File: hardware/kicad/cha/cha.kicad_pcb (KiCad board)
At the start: 4 copper layers, 173 x 134 mm, 137 parts, among them J1 AES_CHA, J2 CONF C, J3 CONF SM, J4 microSD, J5 Câble PROG-CHA, SW1 Retour menu, U1 AMS1117-3.3, U10 74AHCT1G32, U11 74LVC1G07, U12 iCE40HX4K-TQ144, U13 AS4C32M16SB-6TIN, U14 iCE40HX4K-TQ144, U15 IS61WV10248EDBLL-10TLI, U2 AP2112K-1.2, U3 74LVC16244A, U4 74LVC16244A, U5 74LVC16244A, U6 74LVC16244A, U7 74AHCT16244, U8 74AHCT16244, U9 74AHCT244, X1 25 MHz 3,3 V, X2 25 MHz 3,3 V

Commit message: PCB : carte PROG entièrement routée ; CHA à 2 liaisons (DOTA, GAD0)
Routeur de finition : PROG -> dernier raccordement (+3V3 de C46) fait,
plus aucune liaison manquante ; CHA -> P4 routé (et réseaux voisins
rerouttés), restent DOTA et GAD0 dont les broches d'entrée du tampon U7
sont enfermées par les pistes FIXD qui longent sa rangée. DRC des deux
cartes : aucune violation d'isolement ni court-circuit (restent
sérigraphie et bibliothèque non déclarée dans l'environnement).

Co-Authored-By: Claude Opus 5.5 <noreply@anthropic.com>
Claude-Session: https://claude.ai/code/session_01WKfXP1YJ8otGxZ5dsY6Agh
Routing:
- net P4: track 55.6 -> 133.4 mm, vias 2 -> 8
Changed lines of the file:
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@@
   (segment (start 161.5976 95.9844) (end 163.332 94.25) (width 0.127) (layer "B.Cu") (net 193))
   (segment (start 154.235 133.2133) (end 153.7111 133.2133) (width 0.127) (layer "B.Cu") (net 193))
+  (segment (start 121.762499 94.85) (end 121.6625 94.95) (width 0.127) (layer "F.Cu") (net 194))
   (segment (start 181.3375 96.75) (end 181.2283 96.8592) (width 0.127) (layer "F.Cu") (net 194))
   (segment (start 177.5821 128.5995) (end 177.8187 128.8361) (width 0.127) (layer "F.Cu") (net 194))
+  (segment (start 121.9625 94.85) (end 121.762499 94.85) (width 0.127) (layer "F.Cu") (net 194))
+  (segment (start 160.0625 130.05) (end 160.2625 130.05) (width 0.127) (layer "F.Cu") (net 194))
+  (segment (start 121.6625 94.95) (end 121.6625 95.05) (width 0.127) (layer "F.Cu") (net 194))
   (segment (start 161.7792 128.5995) (end 177.5821 128.5995) (width 0.127) (layer "F.Cu") (net 194))
+  (segment (start 134.1625 117.85) (end 134.3625 118.05) (width 0.127) (layer "F.Cu") (net 194))
   (segment (start 181.2283 96.8592) (end 177.5482 96.8592) (width 0.127) (layer "F.Cu") (net 194))
   (segment (start 159.75 130.6287) (end 161.7792 128.5995) (width 0.127) (layer "F.Cu") (net 194))
+  (segment (start 121.5625 103.65) (end 121.5625 105.75) (width 0.127) (layer "F.Cu") (net 194))
+  (segment (start 120.9625 103.05) (end 121.5625 103.65) (width 0.127) (layer "F.Cu") (net 194))
+  (segment (start 121.6625 95.05) (end 121.1625 95.55) (width 0.127) (layer "F.Cu") (net 194))
+  (segment (start 124.262499 117.85) (end 134.1625 117.85) (width 0.127) (layer "F.Cu") (net 194))
+  (segment (start 121.5625 105.75) (end 121.4625 105.85) (width 0.127) (layer "F.Cu") (net 194))
   (segment (start 159.75 131.2875) (end 159.75 130.6287) (width 0.127) (layer "F.Cu") (net 194))
+  (via (at 160.0625 130.05) (size 0.6) (drill 0.3) (layers "F.Cu" "B.Cu") (net 194))
+  (via (at 120.9625 103.05) (size 0.6) (drill 0.3) (layers "F.Cu" "B.Cu") (net 194))
+  (via (at 124.262499 117.85) (size 0.6) (drill 0.3) (layers "F.Cu" "B.Cu") (net 194))
+  (via (at 121.1625 95.55) (size 0.6) (drill 0.3) (layers "F.Cu" "B.Cu") (net 194))
   (via (at 177.8187 128.8361) (size 0.6) (drill 0.3) (layers "F.Cu" "B.Cu") (net 194))
   (via (at 177.5482 96.8592) (size 0.6) (drill 0.3) (layers "F.Cu" "B.Cu") (net 194))
+  (via (at 121.4625 105.85) (size 0.6) (drill 0.3) (layers "F.Cu" "B.Cu") (net 194))
+  (via (at 134.3625 118.05) (size 0.6) (drill 0.3) (layers "F.Cu" "B.Cu") (net 194))
+  (segment (start 158.5625 130.75) (end 158.6625 130.65) (width 0.127) (layer "B.Cu") (net 194))
+  (segment (start 120.9625 97.45) (end 120.8625 97.55) (width 0.127) (layer "B.Cu") (net 194))
+  (segment (start 124.262499 117.25) (end 124.262499 117.85) (width 0.127) (layer "B.Cu") (net 194))
+  (segment (start 156.462499 131.85) (end 156.5625 131.75) (width 0.127) (layer "B.Cu") (net 194))
+  (segment (start 157.0625 131.55) (end 157.1625 131.449999) (width 0.127) (layer "B.Cu") (net 194))
+  (segment (start 120.8625 97.55) (end 120.8625 100.55) (width 0.127) (layer "B.Cu") (net 194))
+  (segment (start 160.0625 130.15) (end 160.0625 130.05) (width 0.127) (layer "B.Cu") (net 194))
+  (segment (start 158.1625 130.949999) (end 158.2625 130.85) (width 0.127) (layer "B.Cu") (net 194))
+  (segment (start 121.4625 105.85) (end 120.1625 107.15) (width 0.127) (layer "B.Cu") (net 194))
+  (segment (start 120.9625 95.95) (end 120.9625 97.45) (width 0.127) (layer "B.Cu") (net 194))
+  (segment (start 139.2625 133.449999) (end 142.9625 133.449999) (width 0.127) (layer "B.Cu") (net 194))
+  (segment (start 154.5625 133.75) (end 155.2625 133.05) (width 0.127) (layer "B.Cu") (net 194))
+  (segment (start 143.2625 133.75) (end 143.3625 133.75) (width 0.127) (layer "B.Cu") (net 194))
+  (segment (start 120.9625 100.65) (end 120.9625 103.05) (width 0.127) (layer "B.Cu") (net 194))
+  (segment (start 158.462499 130.75) (end 158.5625 130.75) (width 0.127) (layer "B.Cu") (net 194))
+  (segment (start 156.1625 132.449999) (end 156.1625 132.05) (width 0.127) (layer "B.Cu") (net 194))
+  (segment (start 137.0625 130.35) (end 137.1625 130.449999) (width 0.127) (layer "B.Cu") (net 194))
+  (segment (start 143.3625 133.85) (end 152.5625 133.85) (width 0.127) (layer "B.Cu") (net 194))
+  (segment (start 122.6625 115.65) (end 124.262499 117.25) (width 0.127) (layer "B.Cu") (net 194))
+  (segment (start 121.1625 95.75) (end 120.9625 95.95) (width 0.127) (layer "B.Cu") (net 194))
+  (segment (start 159.5625 130.55) (end 159.6625 130.55) (width 0.127) (layer "B.Cu") (net 194))
+  (segment (start 156.6625 131.75) (end 156.7625 131.65) (width 0.127) (layer "B.Cu") (net 194))
+  (segment (start 156.3625 131.85) (end 156.462499 131.85) (width 0.127) (layer "B.Cu") (net 194))
+  (segment (start 121.1625 95.55) (end 121.1625 95.75) (width 0.127) (layer "B.Cu") (net 194))
+  (segment (start 157.3625 131.35) (end 157.462499 131.35) (width 0.127) (layer "B.Cu") (net 194))
+  (segment (start 159.4625 130.65) (end 159.5625 130.55) (width 0.127) (layer "B.Cu") (net 194))
+  (segment (start 134.3625 118.05) (end 134.7625 118.45) (width 0.127) (layer "B.Cu") (net 194))
+  (segment (start 155.2625 133.05) (end 155.5625 133.05) (width 0.127) (layer "B.Cu") (net 194))
+  (segment (start 134.7625 118.45) (end 134.7625 127.75) (width 0.127) (layer "B.Cu") (net 194))
+  (segment (start 120.1625 107.15) (end 120.1625 113.15) (width 0.127) (layer "B.Cu") (net 194))
+  (segment (start 156.7625 131.65) (end 156.8625 131.65) (width 0.127) (layer "B.Cu") (net 194))
+  (segment (start 156.962499 131.55) (end 157.0625 131.55) (width 0.127) (layer "B.Cu") (net 194))
+  (segment (start 156.5625 131.75) (end 156.6625 131.75) (width 0.127) (layer "B.Cu") (net 194))
+  (segment (start 121.9625 113.25) (end 122.6625 113.95) (width 0.127) (layer "B.Cu") (net 194))
+  (segment (start 143.3625 133.75) (end 143.3625 133.85) (width 0.127) (layer "B.Cu") (net 194))
+  (segment (start 157.2625 131.449999) (end 157.3625 131.35) (width 0.127) (layer "B.Cu") (net 194))
+  (segment (start 157.7625 131.15) (end 157.8625 131.15) (width 0.127) (layer "B.Cu") (net 194))
+  (segment (start 120.1625 113.15) (end 120.262499 113.25) (width 0.127) (layer "B.Cu") (net 194))
+  (segment (start 142.9625 133.449999) (end 143.2625 133.75) (width 0.127) (layer "B.Cu") (net 194))
+  (segment (start 158.6625 130.65) (end 159.4625 130.65) (width 0.127) (layer "B.Cu") (net 194))
+  (segment (start 157.8625 131.15) (end 158.0625 130.949999) (width 0.127) (layer "B.Cu") (net 194))
   (segment (start 177.8187 128.8361) (end 177.5482 128.5656) (width 0.127) (layer "B.Cu") (net 194))
+  (segment (start 158.0625 130.949999) (end 158.1625 130.949999) (width 0.127) (layer "B.Cu") (net 194))
+  (segment (start 137.0625 130.05) (end 137.0625 130.35) (width 0.127) (layer "B.Cu") (net 194))
+  (segment (start 156.1625 132.05) (end 156.3625 131.85) (width 0.127) (layer "B.Cu") (net 194))
+  (segment (start 156.8625 131.65) (end 156.962499 131.55) (width 0.127) (layer "B.Cu") (net 194))
+  (segment (start 139.1625 132.55) (end 139.1625 133.35) (width 0.127) (layer "B.Cu") (net 194))
+  (segment (start 155.5625 133.05) (end 156.1625 132.449999) (width 0.127) (layer "B.Cu") (net 194))
+  (segment (start 139.1625 133.35) (end 139.2625 133.449999) (width 0.127) (layer "B.Cu") (net 194))
+  (segment (start 158.2625 130.85) (end 158.3625 130.85) (width 0.127) (layer "B.Cu") (net 194))
+  (segment (start 120.8625 100.55) (end 120.9625 100.65) (width 0.127) (layer "B.Cu") (net 194))
+  (segment (start 137.1625 130.55) (end 139.1625 132.55) (width 0.127) (layer "B.Cu") (net 194))
+  (segment (start 152.5625 133.85) (end 152.6625 133.75) (width 0.127) (layer "B.Cu") (net 194))
   (segment (start 177.5482 128.5656) (end 177.5482 96.8592) (width 0.127) (layer "B.Cu") (net 194))
+  (segment (start 157.5625 131.25) (end 157.6625 131.25) (width 0.127) (layer "B.Cu") (net 194))
+  (segment (start 158.3625 130.85) (end 158.462499 130.75) (width 0.127) (layer "B.Cu") (net 194))
+  (segment (start 122.6625 113.95) (end 122.6625 115.65) (width 0.127) (layer "B.Cu") (net 194))
+  (segment (start 157.462499 131.35) (end 157.5625 131.25) (width 0.127) (layer "B.Cu") (net 194))
+  (segment (start 137.1625 130.449999) (end 137.1625 130.55) (width 0.127) (layer "B.Cu") (net 194))
+  (segment (start 134.7625 127.75) (end 137.0625 130.05) (width 0.127) (layer "B.Cu") (net 194))
+  (segment (start 152.6625 133.75) (end 154.5625 133.75) (width 0.127) (layer "B.Cu") (net 194))
+  (segment (start 157.1625 131.449999) (end 157.2625 131.449999) (width 0.127) (layer "B.Cu") (net 194))
+  (segment (start 120.262499 113.25) (end 121.9625 113.25) (width 0.127) (layer "B.Cu") (net 194))
+  (segment (start 157.6625 131.25) (end 157.7625 131.15) (width 0.127) (layer "B.Cu") (net 194))
+  (segment (start 159.6625 130.55) (end 160.0625 130.15) (width 0.127) (layer "B.Cu") (net 194))
   (segment (start 158.75 131.2875) (end 158.75 130.2322) (width 0.127) (layer "F.Cu") (net 195))
   (segment (start 165.1318 95.2812) (end 165.3767 95.0363) (width 0.127) (layer "F.Cu") (net 195))

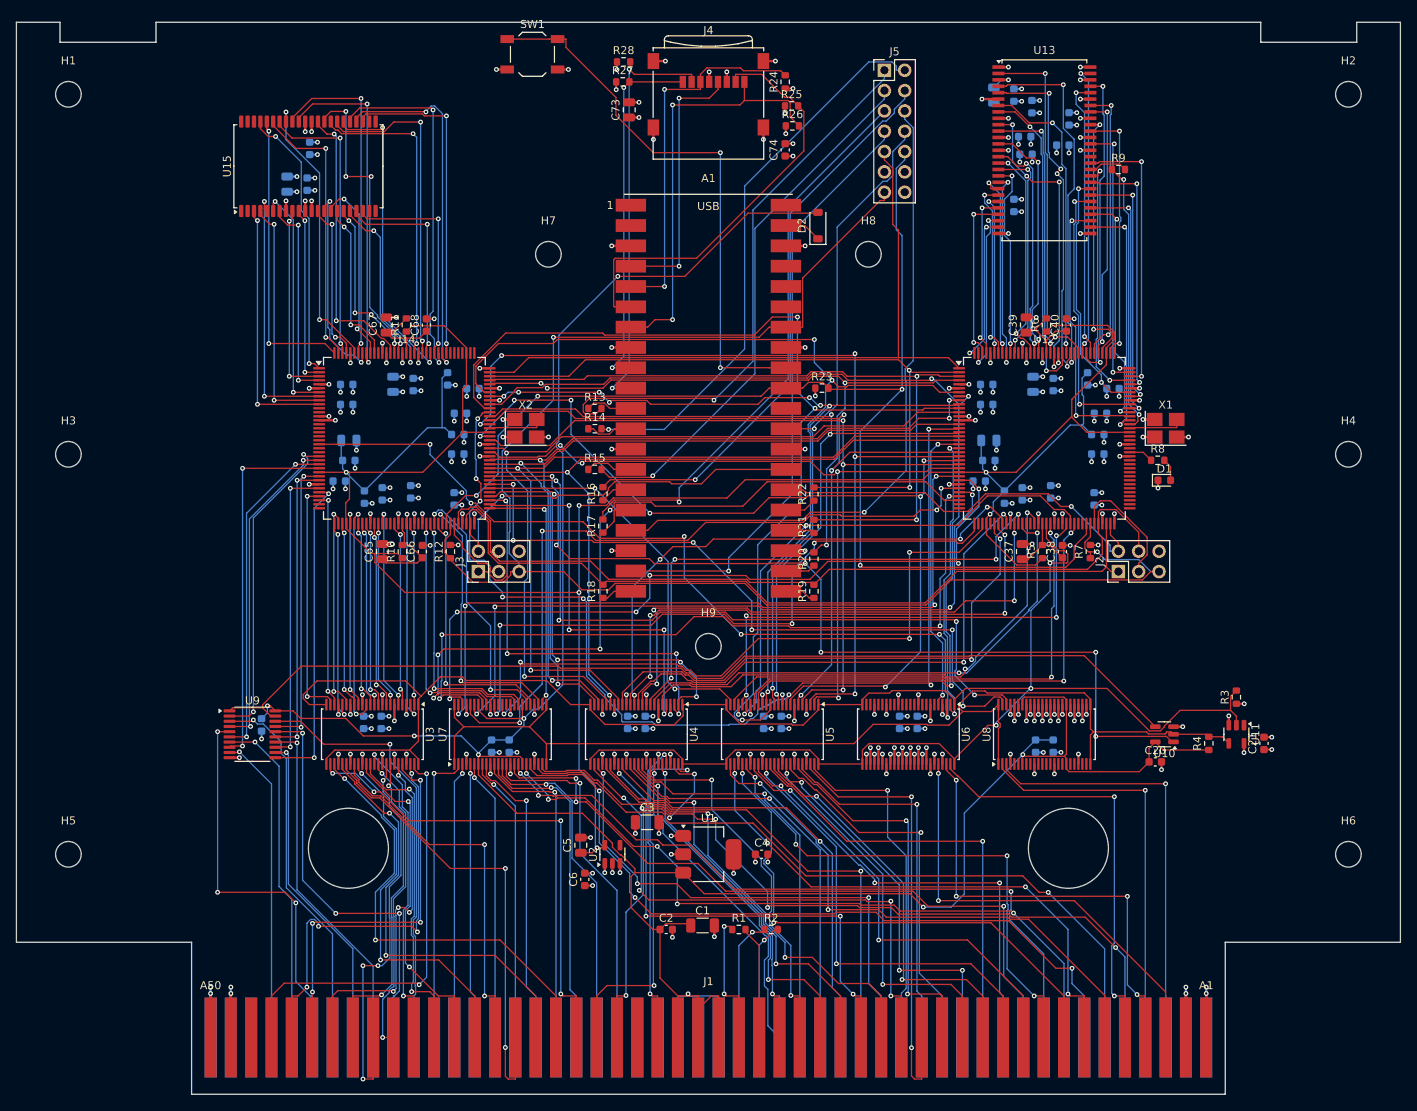
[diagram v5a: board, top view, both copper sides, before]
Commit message: CHA : canaux du tampon de sortie U7 groupés par FPGA source
Couche fixe (FPGA SM) puis sprites (FPGA C), chaque groupe dans l'ordre
des contacts : les deux groupes ne se croisent plus le long de la
rangée d'entrée du tampon, où les pistes FIXD enfermaient DOTA et GAD0.
Broches des FPGA C et SM réoptimisées, carte CHA régénérée (contrôle
Freerouting sans violation) ; nouveau routage en cours.

Co-Authored-By: Claude Opus 5.5 <noreply@anthropic.com>
Claude-Session: https://claude.ai/code/session_01WKfXP1YJ8otGxZ5dsY6Agh
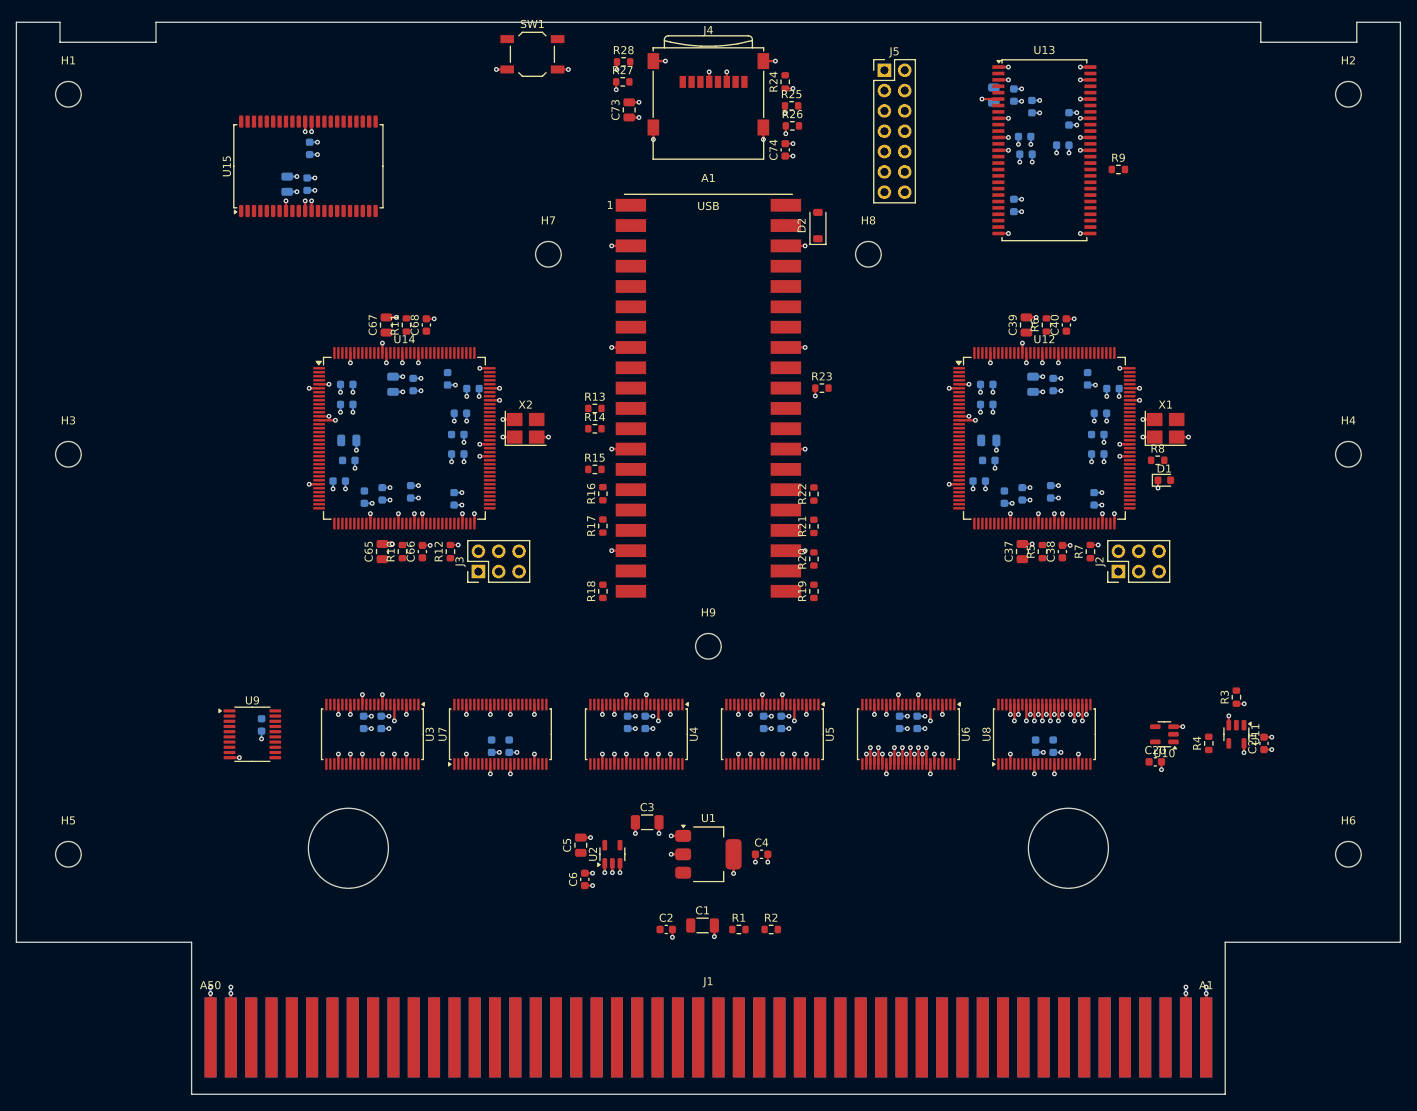
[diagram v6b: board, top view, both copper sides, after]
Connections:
- U12 pad 10: P2 -> P12
- U12 pad 12: P12 -> P10
- U12 pad 39: DOTB -> P17
- U12 pad 41: DOTA -> P16
- U12 pad 42: P17 -> P19
- U12 pad 43: P16 -> P18
- U12 pad 44: P19 -> P21
- U12 pad 45: P18 -> P20
- U12 pad 47: P21 -> P23
- U12 pad 48: P20 -> P22
- U12 pad 49: P23 -> XLAT_EN_N
- U12 pad 52: P22 -> EVEN
- U12 pad 55: XLAT_EN_N -> H
- U12 pad 56: EVEN -> LOAD
- U12 pad 60: H -> CA4
- U12 pad 61: LOAD -> DOTB
- U12 pad 62: CA4 -> DOTA
- U12 pad 8: P1 -> P2
- U12 pad 9: P10 -> P1
- U14 pad 101: P2 -> P1
- U14 pad 74: SDRD0_N -> FIXD1
- U14 pad 75: SDA0 -> FIXD0
- U14 pad 76: SDA1 -> SDRD0_N
- U14 pad 78: 2H1 -> SDA0
- U14 pad 79: FIXD1 -> SDA1
- U14 pad 80: FIXD0 -> 2H1
- U14 pad 85: P10 -> P12
- U14 pad 88: P12 -> P9
- U14 pad 90: P9 -> P10
- U14 pad 99: P1 -> P2
- U7 pad 11: AES_GAD1 -> AES_FIXD1
- U7 pad 12: AES_GAD0 -> AES_FIXD0
- U7 pad 13: AES_DOTB -> AES_GBD3
- U7 pad 14: AES_DOTA -> AES_GBD2
- U7 pad 16: AES_FIXD7 -> AES_GBD1
- U7 pad 17: AES_FIXD6 -> AES_GBD0
- U7 pad 19: AES_FIXD5 -> AES_GAD3
- U7 pad 2: AES_GBD3 -> AES_FIXD7
- U7 pad 20: AES_FIXD4 -> AES_GAD2
- U7 pad 22: AES_FIXD3 -> AES_GAD1
- U7 pad 23: AES_FIXD2 -> AES_GAD0
- U7 pad 26: FIXD2 -> GAD0
- U7 pad 27: FIXD3 -> GAD1
- U7 pad 29: FIXD4 -> GAD2
- U7 pad 3: AES_GBD2 -> AES_FIXD6
- U7 pad 30: FIXD5 -> GAD3
- U7 pad 32: FIXD6 -> GBD0
- U7 pad 33: FIXD7 -> GBD1
- U7 pad 35: DOTA -> GBD2
- U7 pad 36: DOTB -> GBD3
- U7 pad 37: GAD0 -> FIXD0
- U7 pad 38: GAD1 -> FIXD1
- U7 pad 40: GAD2 -> FIXD2
- U7 pad 41: GAD3 -> FIXD3
- U7 pad 43: GBD0 -> FIXD4
- U7 pad 44: GBD1 -> FIXD5
- U7 pad 46: GBD2 -> FIXD6
- U7 pad 47: GBD3 -> FIXD7
- U7 pad 5: AES_GBD1 -> AES_FIXD5
- U7 pad 6: AES_GBD0 -> AES_FIXD4
- U7 pad 8: AES_GAD3 -> AES_FIXD3
- U7 pad 9: AES_GAD2 -> AES_FIXD2
- U8 pad 2: AES_FIXD1 -> AES_DOTB
- U8 pad 3: AES_FIXD0 -> AES_DOTA
- U8 pad 46: FIXD0 -> DOTA
- U8 pad 47: FIXD1 -> DOTB
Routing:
- net +5V: track 348.7 -> 0.00 mm, vias 8 -> 0
- net +1V2: track 304.2 -> 0.00 mm, vias 6 -> 0
- net XLAT_EN_N: track 254.0 -> 0.00 mm, vias 3 -> 0
- net CRESET_N: track 200.4 -> 0.00 mm, vias 2 -> 0
- net CDONE: track 155.0 -> 0.00 mm, vias 4 -> 0
- net OE5_N: track 136.9 -> 0.00 mm
- net P4: track 133.4 -> 0.00 mm, vias 8 -> 0
- net P3: track 128.9 -> 0.00 mm, vias 3 -> 0
- net P1: track 127.3 -> 0.00 mm, vias 3 -> 0
- net SDD_OE5_N: track 125.8 -> 0.00 mm
- net P8: track 117.2 -> 0.00 mm, vias 5 -> 0
- net SDD_OE_N: track 115.7 -> 0.00 mm, vias 6 -> 0
- net P7: track 115.5 -> 0.00 mm, vias 7 -> 0
- net P0: track 114.9 -> 0.00 mm, vias 3 -> 0
- net CHA_IO0: track 105.3 -> 0.00 mm
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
